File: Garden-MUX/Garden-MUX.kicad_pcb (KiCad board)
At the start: 2 copper layers, 46 x 46 mm, 56 parts, among them J1 USB_C_Receptacle_USB2.0_16P, J2 SDCARD_MODULE, P1 S2B-PH-SM4-TB, Q1 AO3401A, U1 ESP32-C6-MINI-1, U2 MCP73832-2-OT, U3 AP2112K-3.3, U4 AP2112K-3.3

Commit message: Update Garden-MUX.kicad_pcb
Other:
- board text added: "AM"
- board text removed: "DESGINED BY ARMANDO MARTINEZ"
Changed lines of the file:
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@@
 			(psa4output no)
 			(plot_black_and_white yes)
+			(plotinvisibletext no)
 			(sketchpadsonfab no)
 			(plotpadnumbers no)
@@
 			(outputformat 1)
 			(mirror no)
-			(drillshape 1)
+			(drillshape 0)
 			(scaleselection 1)
 			(outputdirectory "")
@@
 		(layer "Edge.Cuts")
 	)
-	(gr_text "DESGINED BY ARMANDO MARTINEZ"
-		(at 166.2 106.735 0)
+	(gr_text "AM"
+		(at 155.25 106 0)
 		(layer "B.SilkS" knockout)
 		(effects
@@
 	)
 	(via
-		(at 168.75 79.5)
+		(at 168.75 78.75)
 		(size 0.6)
 		(drill 0.3)
@@
 	)
 	(segment
-		(start 155.050003 95.25)
-		(end 155.050003 93.550003)
-		(width 0.2)
-		(layer "B.Cu")
-		(net 15)
-	)
-	(segment
-		(start 155.050003 93.550003)
-		(end 154.775686 93.275686)
+		(start 151.475 82.190902)
+		(end 147 77.715902)
 		(width 0.2)
 		(layer "B.Cu")
@@
 	)
 	(segment
-		(start 154.775686 91.207488)
-		(end 151.475 87.906802)
+		(start 155 95.199997)
+		(end 155 91.431802)
 		(width 0.2)
 		(layer "B.Cu")
@@
 	)
 	(segment
-		(start 154.775686 93.275686)
-		(end 154.775686 91.207488)
+		(start 147 71.75)
+		(end 146 70.75)
 		(width 0.2)
 		(layer "B.Cu")
@@
 	)
 	(segment
-		(start 151.475 82.190902)
-		(end 147 77.715902)
-		(width 0.2)
-		(layer "B.Cu")
-		(net 15)
-	)
-	(segment
-		(start 147 71.75)
-		(end 146 70.75)
+		(start 155 91.431802)
+		(end 151.475 87.906802)
 		(width 0.2)
 		(layer "B.Cu")

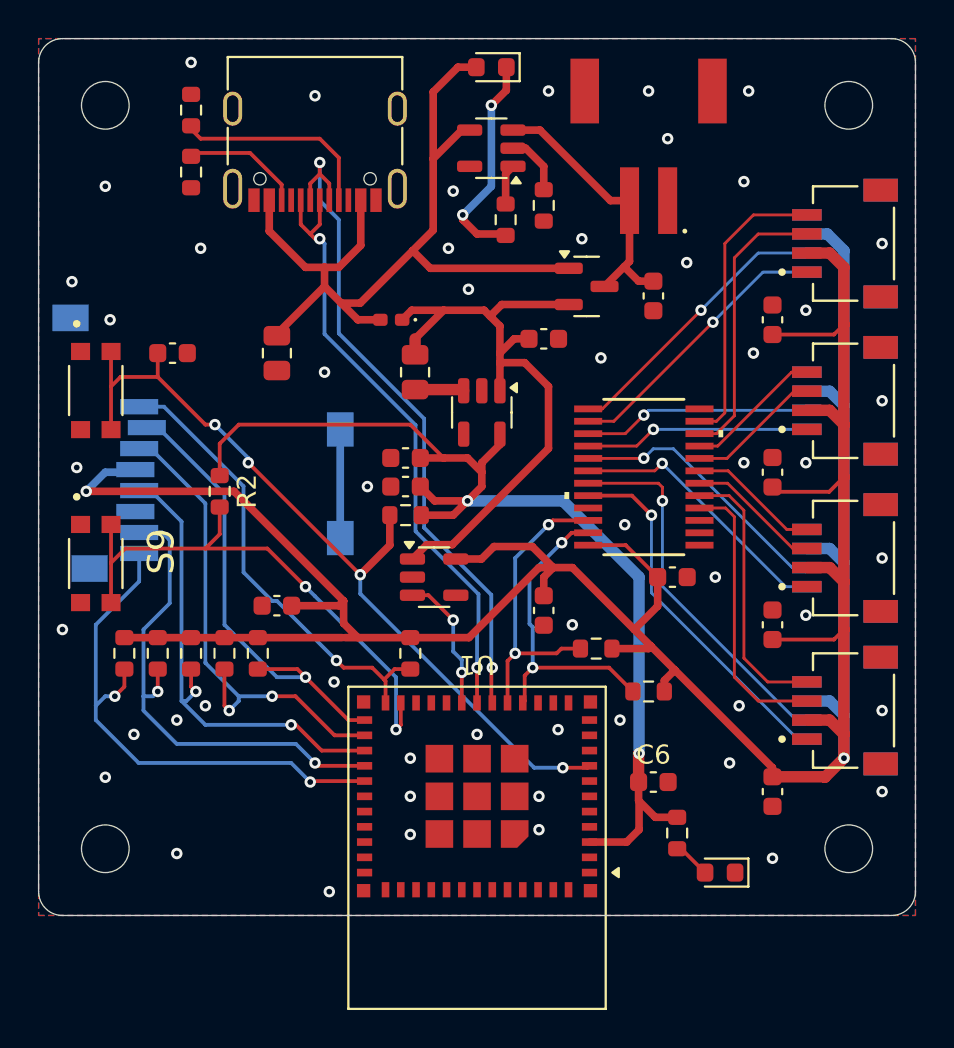
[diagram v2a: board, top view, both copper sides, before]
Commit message: Switch red LED to IO15
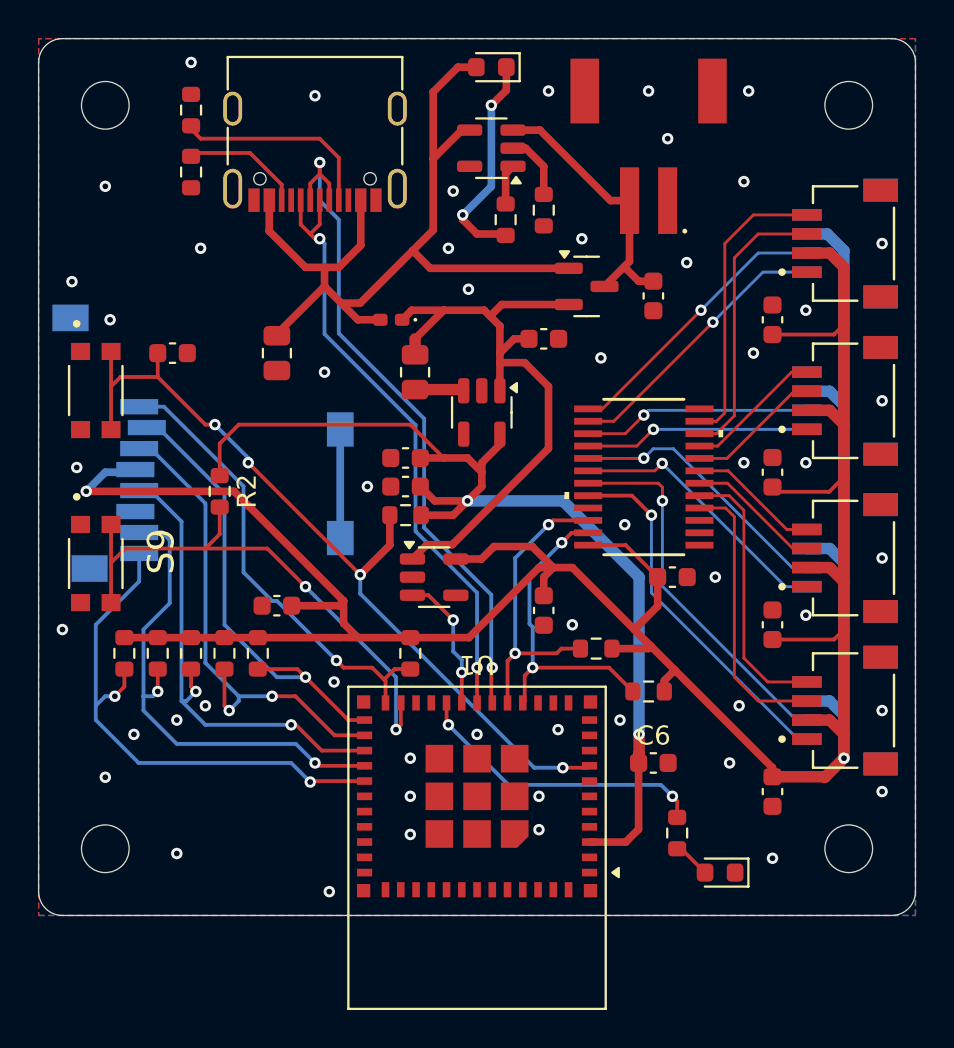
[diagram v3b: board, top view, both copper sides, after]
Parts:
- moved C6 1.00 mm to (163.5, 100.2)
- moved R13 0.25 mm to (157.8, 71.2)
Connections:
- R4 pad 1: +3.3V -> /RED_LED
- U1 pad 20: unconnected-(U1-IO15-Pad20) -> /RED_LED
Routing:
- net /RED_LED: track 0.00 -> 15.7 mm, vias 0 -> 2
- net +3.3V: track 57.0 -> 54.1 mm
